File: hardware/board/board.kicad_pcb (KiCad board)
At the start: 2 copper layers, 20 x 108 mm, 66 parts, among them J1 Power, J10 OUT B3, J12 IN C, J13 OUT C1, J14 OUT C2, J15 OUT C3, J17 OUT D, J18 IN D1, J19 IN D2, J2 IN A, J20 IN D3, J3 OUT A1, J4 OUT A2, J5 OUT A3, J7 IN B, J8 OUT B1, J9 OUT B2, U1 OPA4991, U2 OPA4991, U4 OPA4991, U6 OPA4991

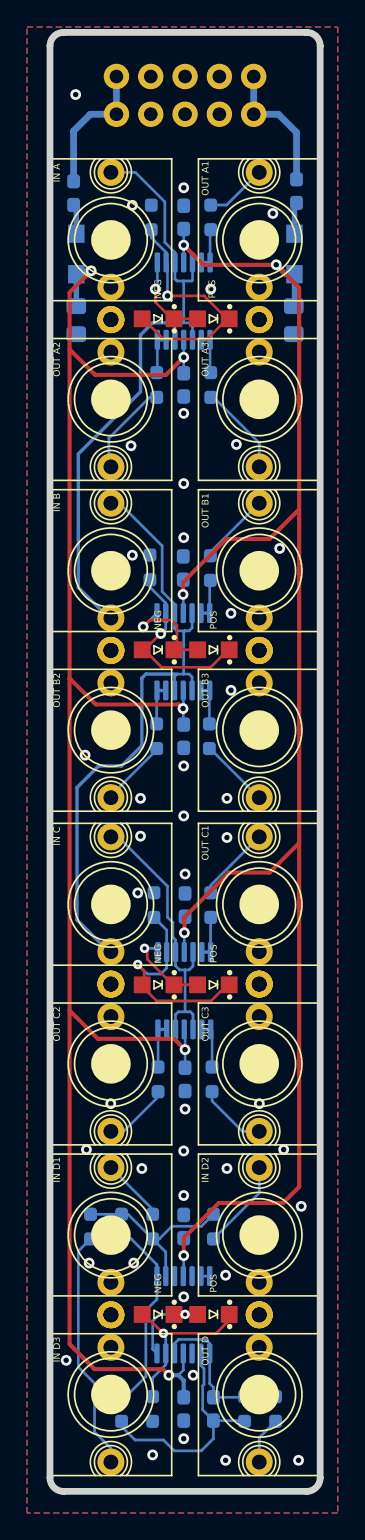
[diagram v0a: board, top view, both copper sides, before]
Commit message: hardware: revision 3
- Update to new Winterbloom footprints
- Update to match current Winterbloom design standards
- Re-route traces
- Update legends
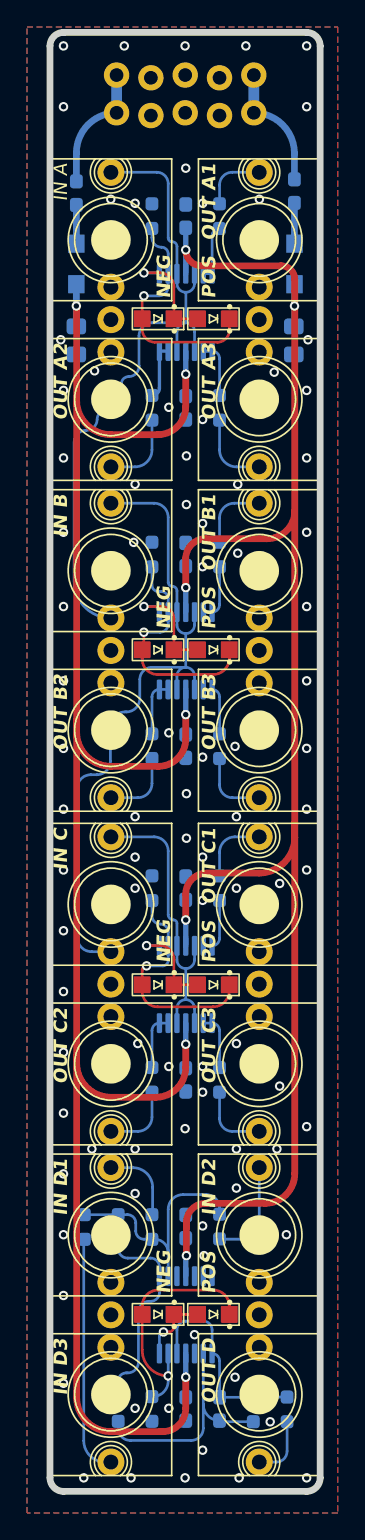
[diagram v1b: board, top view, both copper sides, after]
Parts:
- added ?: , Graphics, B.Cu at (92.4, 112.0)
- C1, C2: value 10uF -> 10u; footprint Capacitor_SMD:C_0805_2012Metric_Pad1.18x1.45mm_HandSolder -> winterbloom:C_0805_HandSolder
- C10, C3, C4, C5, C6, C7, C8, C9: value 0.1uF -> 100n; footprint Capacitor_SMD:C_0603_1608Metric_Pad1.08x0.95mm_HandSolder -> winterbloom:C_0603_HandSolder
- C11: value 12pF -> 12p; footprint Capacitor_SMD:C_0603_1608Metric_Pad1.08x0.95mm_HandSolder -> winterbloom:C_0603_HandSolder
- D1, D2: value BARRIER -> 30V; footprint winterbloom:DIODE_SOD-123_SOD-123F -> winterbloom:D_SOD-123+SOD-123F
- FB1, FB2: value BEAD -> 1k @ 100MHz; footprint Inductor_SMD:L_0603_1608Metric_Pad1.05x0.95mm_HandSolder -> winterbloom:L_0603_HandSolder
- J1: footprint winterbloom:Eurorack_Power -> winterbloom:Eurorack_Power_2x5_Shrouded_Lock
- J10, J14, J15, J17, J20, J4, J5, J9: footprint winterbloom:WQP-WQP518MA-skinny -> winterbloom:AudioJack_WQP518MA_No_S
- J12, J13, J18, J19, J2, J3, J7, J8: footprint winterbloom:WQP-WQP518MA-skinny -> winterbloom:AudioJack_WQP518MA_Compact_S
- R1, R12, R13, R14, R2, R3, R5, R6, R7: value 50R -> 51R; footprint Resistor_SMD:R_0603_1608Metric_Pad0.98x0.95mm_HandSolder -> winterbloom:R_0603_HandSolder
- R10, R11, R15, R16, R18, R19, R20, R4, R8, R9: footprint Resistor_SMD:R_0603_1608Metric_Pad0.98x0.95mm_HandSolder -> winterbloom:R_0603_HandSolder
- R17: value 1k -> 51R; footprint Resistor_SMD:R_0603_1608Metric_Pad0.98x0.95mm_HandSolder -> winterbloom:R_0603_HandSolder
- moved REF** 20.4 mm to (92.6, 100.2)
- moved J1 5.26 mm to (93.8, 51.2)
- moved R3 1.81 mm to (101.5, 75.7)
- moved R2 1.72 mm to (96.5, 75.7)
- moved C4 1.70 mm to (99.0, 75.7)
- moved C1 1.50 mm to (107.0, 70.8)
- moved C2 1.50 mm to (90.8, 70.8), turned to -90 degrees
- moved R12 1.41 mm to (101.5, 111.3)
- moved R11 1.26 mm to (96.5, 111.3)
- moved C7 1.25 mm to (99.0, 111.3)
- moved R5 1.21 mm to (101.5, 86.6)
- moved R7 1.05 mm to (101.5, 100.8)
- moved C5 1.02 mm to (99.0, 86.6)
- moved R10 0.96 mm to (96.5, 86.6)
- moved R17 0.85 mm to (106.5, 149.9)
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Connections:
- C2 pad 1: GND -> -12V
- C2 pad 2: -12V -> GND
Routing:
- net -12V: track 132.5 -> 148.8 mm
- net Net-(D10-A): track 12.8 -> 18.4 mm
- net Net-(U6A--): track 13.8 -> 18.3 mm
- net Net-(J2-Tip): track 47.2 -> 51.3 mm
- net Net-(J12-Tip_normalize): track 47.2 -> 51.2 mm
- net Net-(D5-K): track 13.5 -> 17.5 mm
- net +12V: track 125.7 -> 129.4 mm
- net Net-(U6D-+): track 12.2 -> 15.3 mm
- net Net-(J12-Tip): track 20.6 -> 22.7 mm
- net Net-(D10-K): track 7.18 -> 5.40 mm
- net Net-(R18-Pad1): track 14.1 -> 15.8 mm
- net Net-(J18-Tip): track 4.37 -> 5.84 mm
- net Net-(D3-A): track 6.79 -> 8.08 mm
- net Net-(U2B--): track 3.03 -> 4.29 mm
- net Net-(U1B--): track 3.03 -> 4.29 mm
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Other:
- board text added: "${TITLE} ${REVISION} ${ISSUE_DATE} ${COMMENT2} ${COMMENT3}"
- board text removed: "Helium v2 10/5/2021 CERN-OHL-P V2 helium.wntr.dev"
